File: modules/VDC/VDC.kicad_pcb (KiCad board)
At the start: 2 copper layers, 160 x 100 mm, 2 parts, among them J1 CardConnector

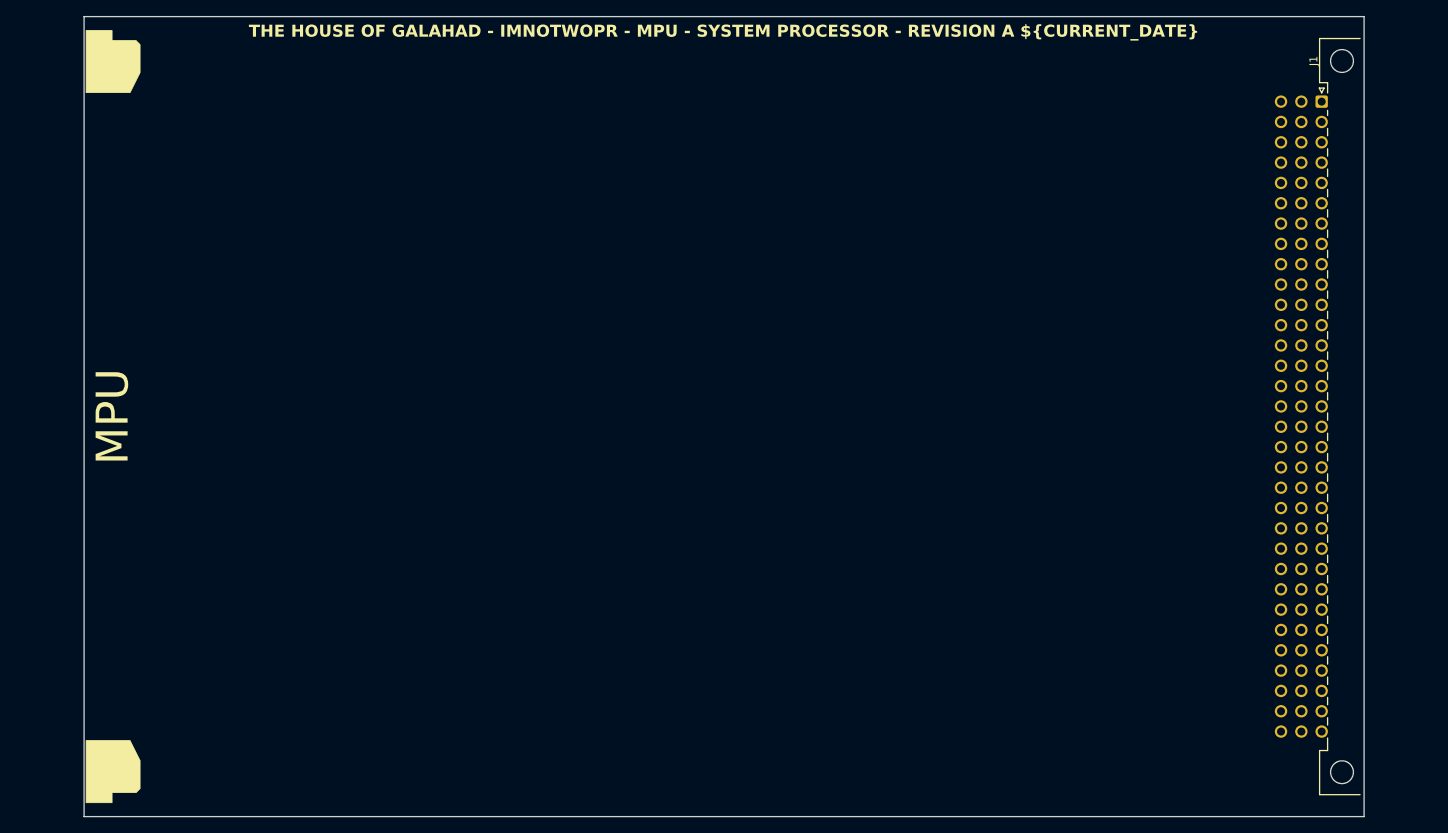
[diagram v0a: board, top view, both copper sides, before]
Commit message: restructure template; stub for vdc & mpu
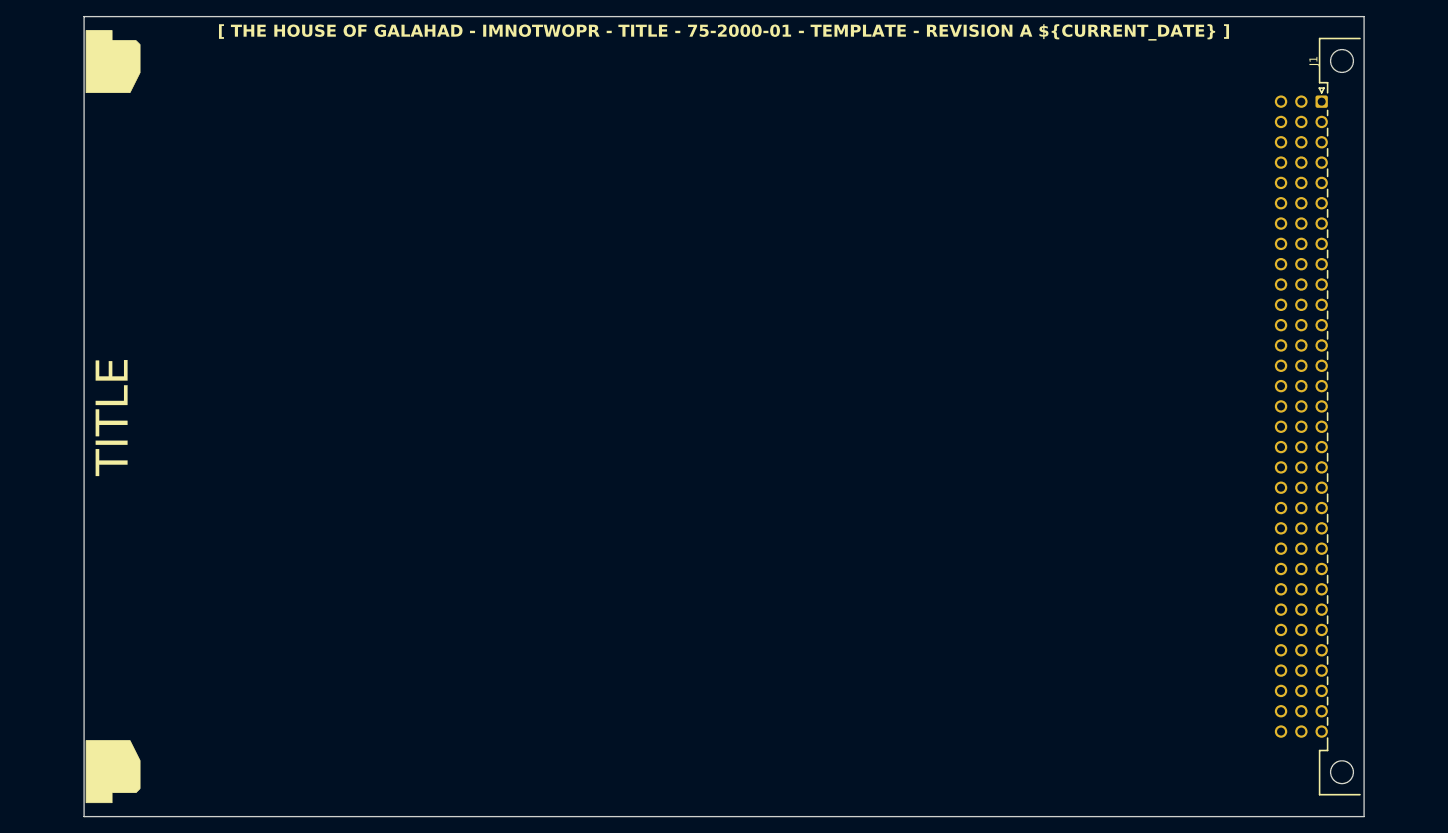
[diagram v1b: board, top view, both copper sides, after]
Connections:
- net VCC renamed +5V
- J1 pad a10: unconnected-(J1A-A_{6}-Pada10) -> /TEMPLATE/S6
- J1 pad a11: unconnected-(J1A-A_{7}-Pada11) -> /TEMPLATE/S7
- J1 pad a12: unconnected-(J1A-A_{8}-Pada12) -> /TEMPLATE/S8
- J1 pad a13: unconnected-(J1A-A_{9}-Pada13) -> /TEMPLATE/S9
- J1 pad a14: unconnected-(J1A-A_{10}-Pada14) -> /TEMPLATE/S10
- J1 pad a15: unconnected-(J1A-A_{11}-Pada15) -> /TEMPLATE/S11
- J1 pad a16: unconnected-(J1A-A_{12}-Pada16) -> /TEMPLATE/S12
- J1 pad a17: unconnected-(J1A-A_{13}-Pada17) -> /TEMPLATE/S13
- J1 pad a18: unconnected-(J1A-A_{14}-Pada18) -> /TEMPLATE/S14
- J1 pad a19: unconnected-(J1A-A_{15}-Pada19) -> /TEMPLATE/S15
- J1 pad a4: unconnected-(J1A-A_{0}-Pada4) -> /TEMPLATE/S0
- J1 pad a5: unconnected-(J1A-A_{1}-Pada5) -> /TEMPLATE/S1
- J1 pad a6: unconnected-(J1A-A_{2}-Pada6) -> /TEMPLATE/S2
- J1 pad a7: unconnected-(J1A-A_{3}-Pada7) -> /TEMPLATE/S3
- J1 pad a8: unconnected-(J1A-A_{4}-Pada8) -> /TEMPLATE/S4
- J1 pad a9: unconnected-(J1A-A_{5}-Pada9) -> /TEMPLATE/S5
- J1 pad c1: GND -> unconnected-(J1C-+5VSB-Padc1)
- J1 pad c3: GND -> unconnected-(J1C-+12V2-Padc3)
- J1 pad c30: GND -> unconnected-(J1C-+12V2-Padc30)
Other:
- board text added: "[ ${COMPANY} - ${COMMENT1} - ${TITLE} - ${COMMENT4} - ${COMMENT2} - REVISION ${REVISION} ${CURRENT_DATE} ]"
- board text removed: "${COMPANY} - ${COMMENT1} - ${TITLE} - ${COMMENT2} - REVISION ${REVISION} ${CURRENT_DATE}"
- board text removed: "Mounting holes are optional Keepout areas are for for guide rails"

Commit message: mpu wip
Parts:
- added J2: Conn_Coaxial, IMNOTWOPR:PanelConnector_1x02, F.Cu at (71.3, 67.1)
- added R1: 470R, IMNOTWOPR:R_Axial_DIN0207_P400mil, F.Cu at (91.6, 62.7)
- added R2: 470R, IMNOTWOPR:R_Axial_DIN0207_P400mil, F.Cu at (91.6, 66.7)
- added R3: 220R, IMNOTWOPR:R_Axial_DIN0207_P400mil, F.Cu at (91.6, 70.6)
- added R4: 820R, IMNOTWOPR:R_Axial_DIN0207_P400mil, F.Cu at (91.6, 74.5)
- added R5: 75R, IMNOTWOPR:R_Axial_DIN0207_P400mil, F.Cu at (91.6, 78.5)
- added U1: 6545, IMNOTWOPR:DIP-40W, F.Cu at (133.5, 95.3)
- added U2: 74HC86, IMNOTWOPR:DIP-14N, F.Cu at (118.3, 76.0)
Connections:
- net /TEMPLATE/S0 renamed /VDC/S0
- net /TEMPLATE/S1 renamed /VDC/S1
- net /TEMPLATE/S10 renamed /VDC/S10
- net /TEMPLATE/S11 renamed /VDC/S11
- net /TEMPLATE/S12 renamed /VDC/S12
- net /TEMPLATE/S13 renamed /VDC/S13
- net /TEMPLATE/S14 renamed /VDC/S14
- net /TEMPLATE/S15 renamed /VDC/S15
- net /TEMPLATE/S2 renamed /VDC/S2
- net /TEMPLATE/S3 renamed /VDC/S3
- net /TEMPLATE/S4 renamed /VDC/S4
- net /TEMPLATE/S5 renamed /VDC/S5
- net /TEMPLATE/S6 renamed /VDC/S6
- net /TEMPLATE/S7 renamed /VDC/S7
- net /TEMPLATE/S8 renamed /VDC/S8
- net /TEMPLATE/S9 renamed /VDC/S9
